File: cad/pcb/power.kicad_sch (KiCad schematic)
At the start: 0 parts

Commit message: finish overview schematic page
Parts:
- added IC?: ISL9110IRT7Z-T7A, SON40P300X300X75-13N, symbol Voltage Regulator:ISL9110IRT7Z-T7A
- added IC?: TCKE812NA,RF, TCKE812NARF, symbol eFuse:TCKE812NA,RF
- added IC?: AP9101CAK6-ABTRG1, SOT95P285X140-6N, symbol Battery Protection:AP9101CAK6-ABTRG1
- added IC?: BQ25040DQCR, SON50P200X300X80-11N, symbol Battery Charger:BQ25040DQCR
- added P?: USB_C_Plug_USB2.0, symbol Connector:USB_C_Plug_USB2.0
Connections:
- new net: P?.A1 (GND), P?.A12 (GND), P?.B1 (GND), P?.B12 (GND)
- new net: P?.A4 (VBUS), P?.A9 (VBUS), P?.B4 (VBUS), P?.B9 (VBUS)
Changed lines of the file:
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@@
     (comment 4 "Simon Brenninger")
   )
+  (symbol (lib_id "Voltage Regulator:ISL9110IRT7Z-T7A") (at 34.29 97.79 0) (unit 1)
+    (in_bom yes) (on_board yes) (fields_autoplaced)
+    (property "Reference" "IC?" (id 0) (at 52.07 90.17 0))
+    (property "Value" "ISL9110IRT7Z-T7A" (id 1) (at 52.07 92.71 0))
+    (property "Footprint" "SON40P300X300X75-13N" (id 2) (at 66.04 95.25 0)
+      (effects (font (size 1.27 1.27)) (justify left) hide)
+    )
+    (property "Datasheet" "https://datasheet.datasheetarchive.com/originals/distributors/Datasheets-SFU4/DSASF4000-1643.pdf" (id 3) (at 66.04 97.79 0)
+      (effects (font (size 1.27 1.27)) (justify left) hide)
+    )
+    (property "Description" "Switching Voltage Regulators 1 2A SINGLE IND BUCK BOOST 3 3V 12LD" (id 4) (at 66.04 100.33 0)
+      (effects (font (size 1.27 1.27)) (justify left) hide)
+    )
+    (property "Height" "0.75" (id 5) (at 66.04 102.87 0)
+      (effects (font (size 1.27 1.27)) (justify left) hide)
+    )
+    (property "Mouser Part Number" "968-ISL9110IRT7Z-T7A" (id 6) (at 66.04 105.41 0)
+      (effects (font (size 1.27 1.27)) (justify left) hide)
+    )
+    (property "Mouser Price/Stock" "https://www.mouser.co.uk/ProductDetail/Renesas-Intersil/ISL9110IRT7Z-T7A?qs=dAsayXGOMrujtMdmCjK0tg%3D%3D" (id 7) (at 66.04 107.95 0)
+      (effects (font (size 1.27 1.27)) (justify left) hide)
+    )
+    (property "Manufacturer_Name" "Renesas Electronics" (id 8) (at 66.04 110.49 0)
+      (effects (font (size 1.27 1.27)) (justify left) hide)
+    )
+    (property "Manufacturer_Part_Number" "ISL9110IRT7Z-T7A" (id 9) (at 66.04 113.03 0)
+      (effects (font (size 1.27 1.27)) (justify left) hide)
+    )
+    (pin "1")
+    (pin "10")
+    (pin "11")
+    (pin "12")
+    (pin "13")
+    (pin "2")
+    (pin "3")
+    (pin "4")
+    (pin "5")
+    (pin "6")
+    (pin "7")
+    (pin "8")
+    (pin "9")
+  )
+  (symbol (lib_id "Connector:USB_C_Plug_USB2.0") (at 38.1 45.72 0) (unit 1)
+    (in_bom yes) (on_board yes) (fields_autoplaced)
+    (property "Reference" "P?" (id 0) (at 38.1 22.86 0))
+    (property "Value" "USB_C_Plug_USB2.0" (id 1) (at 38.1 25.4 0))
+    (property "Footprint" "" (id 2) (at 41.91 45.72 0)
+      (effects (font (size 1.27 1.27)) hide)
+    )
+    (property "Datasheet" "https://www.usb.org/sites/default/files/documents/usb_type-c.zip" (id 3) (at 41.91 45.72 0)
+      (effects (font (size 1.27 1.27)) hide)
+    )
+    (pin "A1")
+    (pin "A12")
+    (pin "A4")
+    (pin "A5")
+    (pin "A6")
+    (pin "A7")
+    (pin "A9")
+    (pin "B1")
+    (pin "B12")
+    (pin "B4")
+    (pin "B5")
+    (pin "B9")
+    (pin "S1")
+  )
+  (symbol (lib_id "eFuse:TCKE812NA,RF") (at 215.9 46.99 0) (unit 1)
+    (in_bom yes) (on_board yes) (fields_autoplaced)
+    (property "Reference" "IC?" (id 0) (at 235.6994 72.39 0)
+      (effects (font (size 1.27 1.27)) (justify left))
+    )
+    (property "Value" "TCKE812NA,RF" (id 1) (at 235.6994 74.93 0)
+      (effects (font (size 1.27 1.27)) (justify left))
+    )
+    (property "Footprint" "TCKE812NARF" (id 2) (at 247.65 34.29 0)
+      (effects (font (size 1.27 1.27)) (justify left) hide)
+    )
+    (property "Datasheet" "https://www.arrow.com/en/products/tcke812narf/toshiba" (id 3) (at 247.65 36.83 0)
+      (effects (font (size 1.27 1.27)) (justify left) hide)
+    )
+    (property "Description" "Hot Swap Voltage Controllers 15.1V VOLTAGE CLMP AUTO RETRY" (id 4) (at 247.65 39.37 0)
+      (effects (font (size 1.27 1.27)) (justify left) hide)
+    )
+    (property "Height" "0.75" (id 5) (at 247.65 41.91 0)
+      (effects (font (size 1.27 1.27)) (justify left) hide)
+    )
+    (property "Mouser Part Number" "757-TCKE812NA,RF" (id 6) (at 247.65 44.45 0)
+      (effects (font (size 1.27 1.27)) (justify left) hide)
+    )
+    (property "Mouser Price/Stock" "https://www.mouser.co.uk/ProductDetail/Toshiba/TCKE812NARF?qs=7MVldsJ5UazIz%2F5VEH%2F60g%3D%3D" (id 7) (at 247.65 46.99 0)
+      (effects (font (size 1.27 1.27)) (justify left) hide)
+    )
+    (property "Manufacturer_Name" "Toshiba" (id 8) (at 247.65 49.53 0)
+      (effects (font (size 1.27 1.27)) (justify left) hide)
+    )
+    (property "Manufacturer_Part_Number" "TCKE812NA,RF" (id 9) (at 247.65 52.07 0)
+      (effects (font (size 1.27 1.27)) (justify left) hide)
+    )
+    (pin "1")
+    (pin "10")
+    (pin "11")
+    (pin "12")
+    (pin "13")
+    (pin "14")
+    (pin "15")
+    (pin "2")
+    (pin "3")
+    (pin "4")
+    (pin "5")
+    (pin "6")
+    (pin "7")
+    (pin "8")
+    (pin "9")
+  )
+  (symbol (lib_id "Battery Protection:AP9101CAK6-ABTRG1") (at 162.56 45.72 0) (unit 1)
+    (in_bom yes) (on_board yes) (fields_autoplaced)
+    (property "Reference" "IC?" (id 0) (at 175.26 38.1 0))
+    (property "Value" "AP9101CAK6-ABTRG1" (id 1) (at 175.26 40.64 0))
+    (property "Footprint" "SOT95P285X140-6N" (id 2) (at 184.15 43.18 0)
+      (effects (font (size 1.27 1.27)) (justify left) hide)
+    )
+    (property "Datasheet" "https://www.diodes.com/assets/Datasheets/AP9101C.pdf" (id 3) (at 184.15 45.72 0)
+      (effects (font (size 1.27 1.27)) (justify left) hide)
+    )
+    (property "Description" "Battery Management Protection IC 1-Cell LI 3.0uA 3.5V" (id 4) (at 184.15 48.26 0)
+      (effects (font (size 1.27 1.27)) (justify left) hide)
+    )
+    (property "Height" "1.4" (id 5) (at 184.15 50.8 0)
+      (effects (font (size 1.27 1.27)) (justify left) hide)
+    )
+    (property "Mouser Part Number" "621-AP9101CAK6ABTRG1" (id 6) (at 184.15 53.34 0)
+      (effects (font (size 1.27 1.27)) (justify left) hide)
+    )
+    (property "Mouser Price/Stock" "https://www.mouser.co.uk/ProductDetail/Diodes-Incorporated/AP9101CAK6-ABTRG1?qs=W66WzN12R3Y9HS2QV9IuJA%3D%3D" (id 7) (at 184.15 55.88 0)
+      (effects (font (size 1.27 1.27)) (justify left) hide)
+    )
+    (property "Manufacturer_Name" "Diodes Inc." (id 8) (at 184.15 58.42 0)
+      (effects (font (size 1.27 1.27)) (justify left) hide)
+    )
+    (property "Manufacturer_Part_Number" "AP9101CAK6-ABTRG1" (id 9) (at 184.15 60.96 0)
+      (effects (font (size 1.27 1.27)) (justify left) hide)
+    )
+    (pin "1")
+    (pin "2")
+    (pin "3")
+    (pin "4")
+    (pin "5")
+    (pin "6")
+  )
+  (symbol (lib_id "Battery Charger:BQ25040DQCR") (at 92.71 40.64 0) (unit 1)
+    (in_bom yes) (on_board yes) (fields_autoplaced)
+    (property "Reference" "IC?" (id 0) (at 110.49 33.02 0))
+    (property "Value" "BQ25040DQCR" (id 1) (at 110.49 35.56 0))
+    (property "Footprint" "SON50P200X300X80-11N" (id 2) (at 124.46 38.1 0)
+      (effects (font (size 1.27 1.27)) (justify left) hide)
+    )
+    (property "Datasheet" "http://www.ti.com/lit/gpn/bq25040" (id 3) (at 124.46 40.64 0)
+      (effects (font (size 1.27 1.27)) (justify left) hide)
+    )
+    (property "Description" "1.1A, Single-Input, Single Cell Li-Ion Battery Charger With 50mA LDO in 2x3 QFN" (id 4) (at 124.46 43.18 0)
+      (effects (font (size 1.27 1.27)) (justify left) hide)
+    )
+    (property "Height" "0.8" (id 5) (at 124.46 45.72 0)
+      (effects (font (size 1.27 1.27)) (justify left) hide)
+    )
+    (property "Mouser Part Number" "595-BQ25040DQCR" (id 6) (at 124.46 48.26 0)
+      (effects (font (size 1.27 1.27)) (justify left) hide)
+    )
+    (property "Mouser Price/Stock" "https://www.mouser.co.uk/ProductDetail/Texas-Instruments/BQ25040DQCR?qs=LWWr1WFOkdGauR4seMHvtw%3D%3D" (id 7) (at 124.46 50.8 0)
+      (effects (font (size 1.27 1.27)) (justify left) hide)
+    )
+    (property "Manufacturer_Name" "Texas Instruments" (id 8) (at 124.46 53.34 0)
+      (effects (font (size 1.27 1.27)) (justify left) hide)
+    )
+    (property "Manufacturer_Part_Number" "BQ25040DQCR" (id 9) (at 124.46 55.88 0)
+      (effects (font (size 1.27 1.27)) (justify left) hide)
+    )
+    (pin "1")
+    (pin "10")
+    (pin "11")
+    (pin "2")
+    (pin "3")
+    (pin "4")
+    (pin "5")
+    (pin "6")
+    (pin "7")
+    (pin "8")
+    (pin "9")
+  )
 )

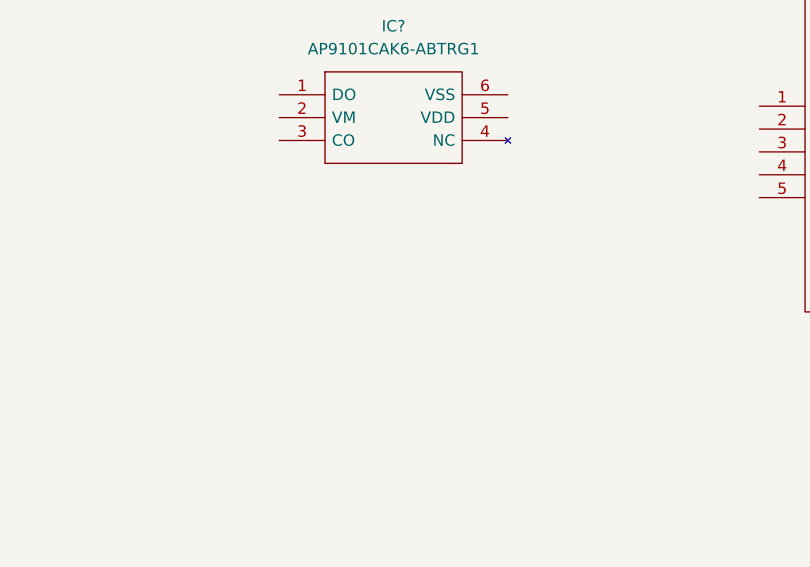
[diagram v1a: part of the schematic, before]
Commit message: finish mcu connections
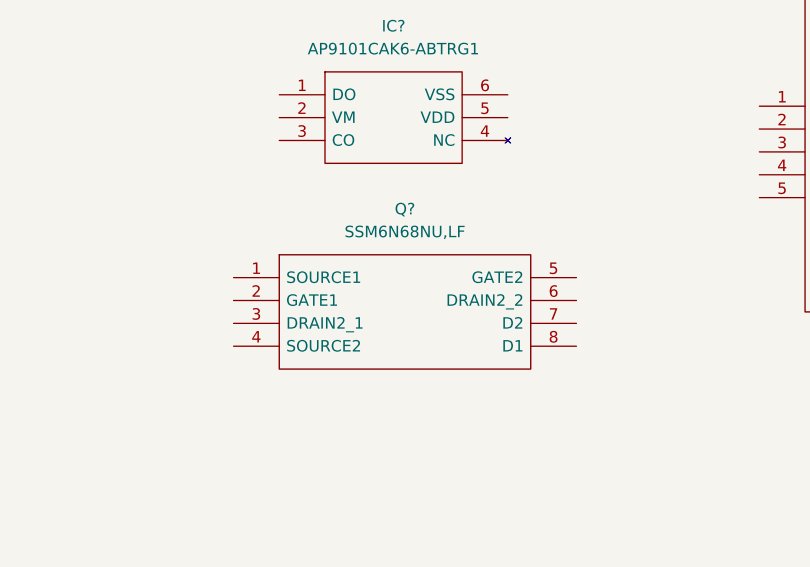
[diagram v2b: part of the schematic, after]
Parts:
- added Q?: SSM6N68NU,LF, SSM6N68NULF, symbol MOSFET:SSM6N68NU,LF
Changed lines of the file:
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@@
     (pin "9")
+  )
+  (symbol (lib_id "MOSFET:SSM6N68NU,LF") (at 157.48 66.04 0) (unit 1)
+    (in_bom yes) (on_board yes) (fields_autoplaced)
+    (property "Reference" "Q?" (id 0) (at 176.53 58.42 0))
+    (property "Value" "SSM6N68NU,LF" (id 1) (at 176.53 60.96 0))
+    (property "Footprint" "SSM6N68NULF" (id 2) (at 191.77 63.5 0)
+      (effects (font (size 1.27 1.27)) (justify left) hide)
+    )
+    (property "Datasheet" "http://toshiba.semicon-storage.com/info/docget.jsp?did=60465&prodName=SSM6N68NU" (id 3) (at 191.77 66.04 0)
+      (effects (font (size 1.27 1.27)) (justify left) hide)
+    )
+    (property "Description" "MOSFET LowON Res MOSFET ID=4A VDSS=30V" (id 4) (at 191.77 68.58 0)
+      (effects (font (size 1.27 1.27)) (justify left) hide)
+    )
+    (property "Height" "0.8" (id 5) (at 191.77 71.12 0)
+      (effects (font (size 1.27 1.27)) (justify left) hide)
+    )
+    (property "Mouser2 Part Number" "" (id 6) (at 191.77 73.66 0)
+      (effects (font (size 1.27 1.27)) (justify left) hide)
+    )
+    (property "Mouser2 Price/Stock" "" (id 7) (at 191.77 76.2 0)
+      (effects (font (size 1.27 1.27)) (justify left) hide)
+    )
+    (property "Manufacturer_Name" "Toshiba" (id 8) (at 191.77 78.74 0)
+      (effects (font (size 1.27 1.27)) (justify left) hide)
+    )
+    (property "Manufacturer_Part_Number" "SSM6N68NU,LF" (id 9) (at 191.77 81.28 0)
+      (effects (font (size 1.27 1.27)) (justify left) hide)
+    )
+    (pin "1")
+    (pin "2")
+    (pin "3")
+    (pin "4")
+    (pin "5")
+    (pin "6")
+    (pin "7")
+    (pin "8")
   )
   (symbol (lib_id "Battery Protection:AP9101CAK6-ABTRG1") (at 162.56 45.72 0) (unit 1)

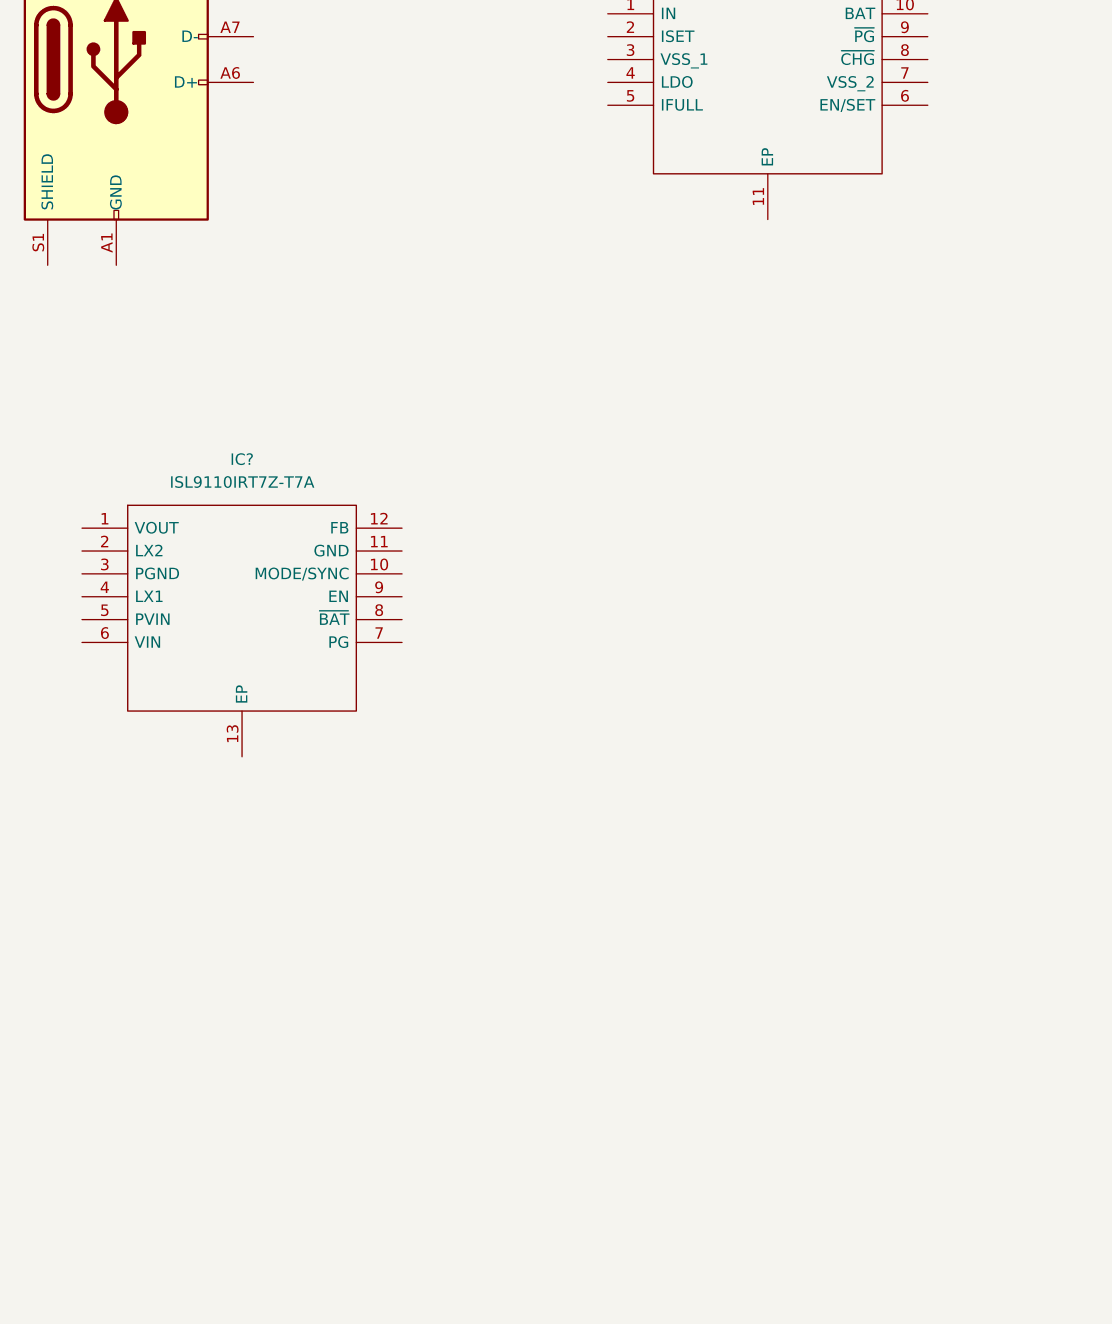
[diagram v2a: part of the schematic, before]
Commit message: changed MCU package
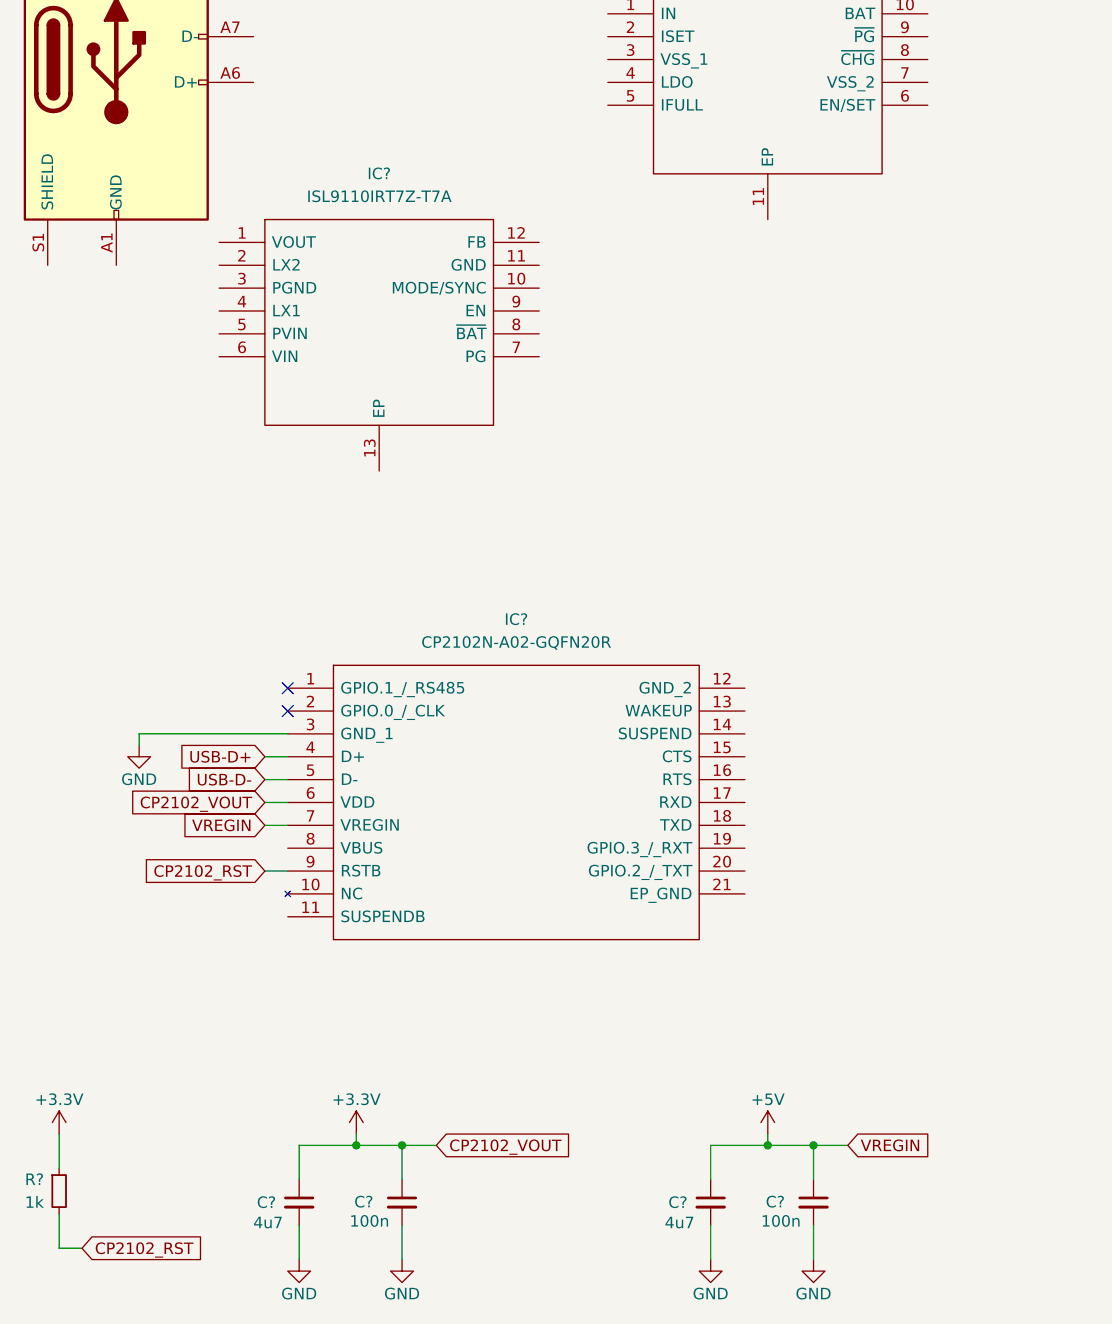
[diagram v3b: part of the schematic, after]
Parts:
- added C? (x2): 4u7, symbol Device:C_Small
- added C? (x2): 100n, symbol Device:C_Small
- added IC?: CP2102N-A02-GQFN20R, CP2102NA02GQFN20, symbol USB-UART Bridge:CP2102N-A02-GQFN20R
- added R?: 1k, symbol Device:R_Small
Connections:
- new net +3.3V: C?.1, C?.1, IC?.6 (VDD), R?.1
- new net +5V: C?.1, C?.1, IC?.7 (VREGIN)
- new net CP2102_RST: IC?.9 (RSTB), R?.2
- new net GND: C?.2, C?.2, C?.2, C?.2, IC?.3 (GND_1)
- new net USB-D+: IC?.4 (D+)
- new net USB-D-: IC?.5 (D-)
- no-connect marks 0 -> 2
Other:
- moved on the sheet: IC?
